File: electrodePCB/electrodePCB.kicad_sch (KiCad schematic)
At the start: 18 parts, among them J1 Conn_01x16_Pin, U1 TMP119AIYBGR

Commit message: still in the middle of it, but added the 20p, 2 additional heaters (including adjustable postition) and begining to define pinout
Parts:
- removed J1: Conn_01x16_Pin, MOLEX FPC:CON_5034801600_MOL, symbol Connector:Conn_01x16_Pin
- added J1: Conn_01x20, 5034802000 FPC Molex:CON_5034802000_MOL, symbol Connector_Generic:Conn_01x20
- added R10, R8, R9: R_US, Resistor_SMD:R_0603_1608Metric, symbol Device:R_US
- R2: renamed from R6; footprint Resistor_SMD:R_2512_6332Metric_Pad1.40x3.35mm_HandSolder -> Resistor_SMD:adjustable
- renumbered E1 to E0, E2 to E1, E3 to E2, E4 to E3, E5 to E4, E6 to E5, R7 to R3, R3 to R4, R2 to R5, R4 to R6, R5 to R7
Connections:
- net +3V3: now also J1.11 (Pin_11)
- net GND: now also R1.2, R2.2, R3.2, J1.14 (Pin_14), J1.15 (Pin_15), J1.17 (Pin_17), J1.19 (Pin_19), R10.1, R8.1, R9.1
- net SCL: now also J1.13 (Pin_13)
- net SDA: now also J1.12 (Pin_12)
- net at E0.1 (Pin_1): now also J1.1 (Pin_1), R8.2
- net at E2.1 (Pin_1): now also J1.3 (Pin_3), R10.2
- net at E1.1 (Pin_1): now also J1.2 (Pin_2), R9.2
- net at E3.1 (Pin_1): now also J1.4 (Pin_4)
- net at R1.1: now also J1.20 (Pin_20)
- net at S1.1 (Pin_1): now also J1.7 (Pin_7)
- net at S1.2 (Pin_2): now also J1.8 (Pin_8)
- net at S1.3 (Pin_3): now also J1.9 (Pin_9)
- net at S1.4 (Pin_4): now also J1.10 (Pin_10)
- net at E4.1 (Pin_1): now also J1.5 (Pin_5)
- net at E5.1 (Pin_1): now also J1.6 (Pin_6)
- net at R3.1: now also J1.16 (Pin_16)
- net at R2.1: now also J1.18 (Pin_18)
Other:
- moved on the sheet: R1, R2, R3

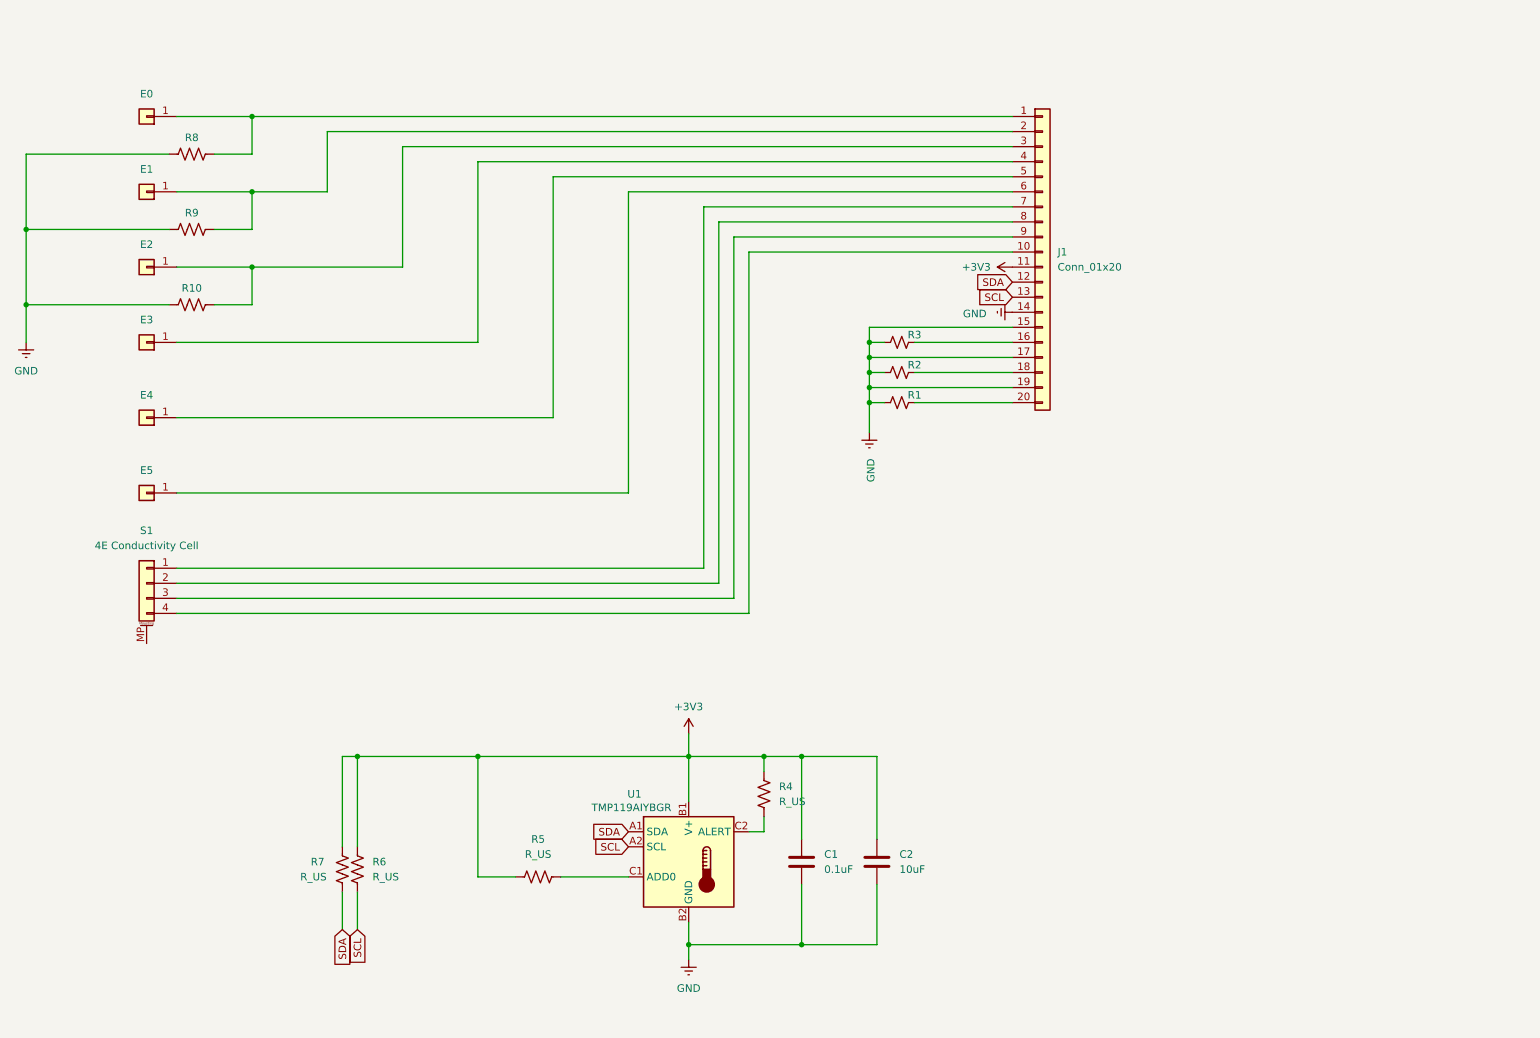
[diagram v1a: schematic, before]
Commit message: bunch of routing, adapted interconnect pinout to accomedate routing. Added GND plane.
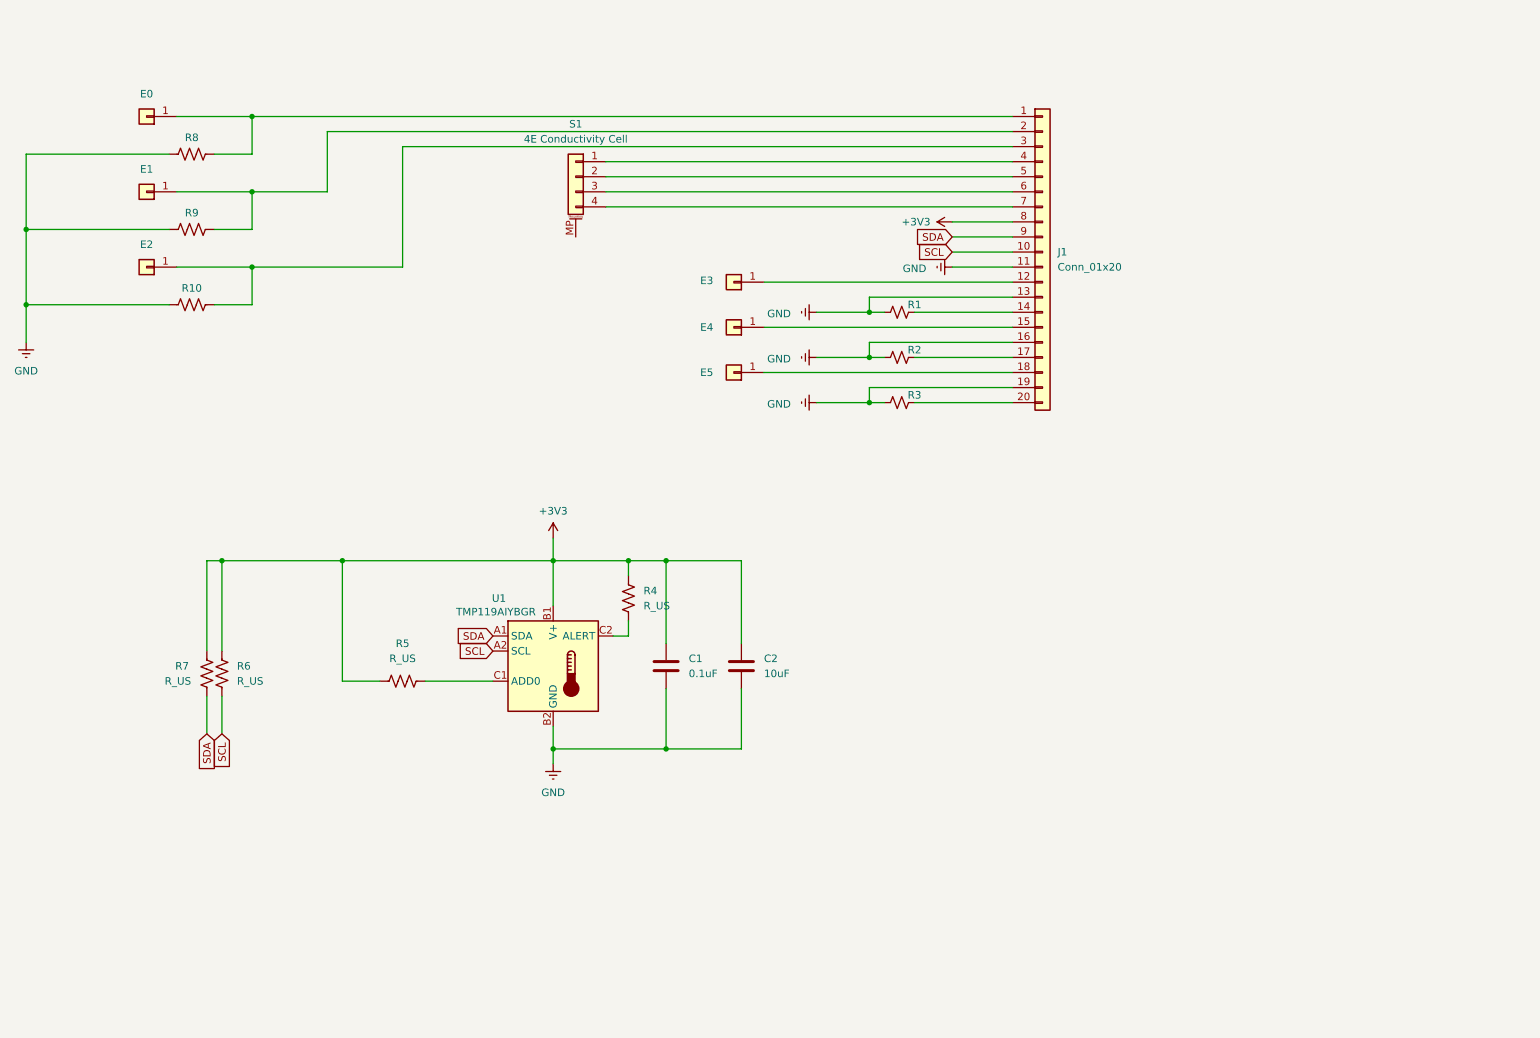
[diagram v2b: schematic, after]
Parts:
- R6, R7: footprint Resistor_SMD:R_0603_1608Metric -> Resistor_SMD:R_0402_1005Metric
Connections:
- net +3V3: now also J1.8 (Pin_8); no longer J1.11 (Pin_11)
- net GND: now also J1.11 (Pin_11), J1.13 (Pin_13), J1.16 (Pin_16); no longer J1.14 (Pin_14), J1.15 (Pin_15), J1.17 (Pin_17)
- net SCL: now also J1.10 (Pin_10); no longer J1.13 (Pin_13)
- net SDA: now also J1.9 (Pin_9); no longer J1.12 (Pin_12)
- net at E3.1 (Pin_1): now also J1.12 (Pin_12); no longer J1.4 (Pin_4)
- net at R1.1: now also J1.14 (Pin_14); no longer J1.20 (Pin_20)
- net at E4.1 (Pin_1): now also J1.15 (Pin_15); no longer J1.5 (Pin_5)
- net at R3.1: now also J1.20 (Pin_20); no longer J1.16 (Pin_16)
- net at R2.1: now also J1.17 (Pin_17); no longer J1.18 (Pin_18)
- net at E5.1 (Pin_1): now also J1.18 (Pin_18); no longer J1.6 (Pin_6)
- net at S1.4 (Pin_4): now also J1.7 (Pin_7); no longer J1.10 (Pin_10)
- net at S1.1 (Pin_1): now also J1.4 (Pin_4); no longer J1.7 (Pin_7)
- net at S1.2 (Pin_2): now also J1.5 (Pin_5); no longer J1.8 (Pin_8)
- net at S1.3 (Pin_3): now also J1.6 (Pin_6); no longer J1.9 (Pin_9)
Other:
- moved on the sheet: C1, C2, E3, E4, E5, R1, R2, R3, R4, R5, R6, R7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

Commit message: routing, routing, routing. We removed one of the three heaters and decided to displace the other two and route to rings around the electrodes. I verified the temperature sensor is work!
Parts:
- removed R2: R_Small_US, Resistor_SMD:adjustable, symbol Device:R_Small_US
- added J2: qwiic, Connector_JST:JST_SH_BM04B-SRSS-TB_1x04-1MP_P1.00mm_Vertical, symbol Connector_Generic_MountingPin:Conn_01x04_MountingPin
- J1: value Conn_01x20 -> FPC 20p
- R1, R3: footprint Resistor_SMD:R_2512_6332Metric_Pad1.40x3.35mm_HandSolder -> Resistor_SMD:R_2010_5025Metric
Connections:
- net +3V3: now also J2.2 (Pin_2)
- net GND: now also J1.15 (Pin_15), J2.1 (Pin_1); no longer J1.13 (Pin_13), J1.16 (Pin_16)
- net SCL: now also J2.4 (Pin_4)
- net SDA: now also J2.3 (Pin_3)
- net at E3.1 (Pin_1): now also J1.14 (Pin_14); no longer J1.12 (Pin_12)
- net at R1.1: now also J1.18 (Pin_18); no longer J1.14 (Pin_14)
- net at E4.1 (Pin_1): now also J1.17 (Pin_17); no longer J1.15 (Pin_15)
- net at R3.1: now also J1.16 (Pin_16); no longer J1.20 (Pin_20)
- net at E5.1 (Pin_1): now also J1.20 (Pin_20); no longer J1.18 (Pin_18)
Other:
- moved on the sheet: E0, E1, E2, E3, E4, E5, J1, R1, R10, R3, R8, R9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

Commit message: routing and more routing. still working, but add thermal rings. added qwiic.
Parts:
- removed C2: 10uF, Capacitor_SMD:C_0603_1608Metric, symbol Device:C
- R4, R5: footprint Resistor_SMD:R_0603_1608Metric -> Resistor_SMD:R_0402_1005Metric
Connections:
- net +3V3: now also J1.10 (Pin_10); no longer J1.8 (Pin_8)
- net SCL: now also J1.8 (Pin_8); no longer J1.10 (Pin_10)
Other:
- moved on the sheet: J2

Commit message: roughly finalized layout. Might tidy up the GND plane with some keep outs
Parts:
- R0: renamed from R8; value R_US -> 0 ohm
- R4, R7: value R_US -> 10k
- R6: renamed from R5; value R_US -> 10k
- R8: renamed from R6; value R_US -> 10k
- renumbered R9 to R1, R10 to R2, R1 to R5
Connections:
- net at E3.1 (Pin_1): now also J1.12 (Pin_12); no longer J1.14 (Pin_14)
- net at J1.18 (Pin_18), R5.1: now also J1.17 (Pin_17)
- net at E4.1 (Pin_1): now also J1.16 (Pin_16); no longer J1.17 (Pin_17)
- net at R3.1: now also J1.13 (Pin_13), J1.14 (Pin_14); no longer J1.16 (Pin_16)
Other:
- note added: "3 typical reference electrodes (E0-E2)"
- note added: "4E conductivity cell"
- note added: "Electrodes (E3-E5) typically ISEs"
- note added: "Main interconnect"
- note added: "Qwiic Connector"
- note added: "Temperature Sensor"
- company: (none) -> William Pardis
- title: (none) -> electrodePCB
- moved on the sheet: C1, E0, E1, E2, E3, E4, E5, J1, J2, R0, R1, R2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

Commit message: labeling of the Cond Cell
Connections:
- net force 1: now reaches J1.4 (Pin_4), S1.1 (Pin_1)
- net Sense 1: now reaches J1.5 (Pin_5), S1.2 (Pin_2)
- net Sense 2: now reaches J1.6 (Pin_6), S1.3 (Pin_3)
- net force 2: now reaches J1.7 (Pin_7), S1.4 (Pin_4)
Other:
- note removed: "4E conductivity cell"
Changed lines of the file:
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@@
-		)
-	)
-	(text "4E conductivity cell"
-		(exclude_from_sim no)
-		(at 112.522 80.772 0)
-		(effects
-			(font
-				(face "Arial Black")
-				(size 2.54 2.54)
-				(bold yes)
-			)
-			(justify left)
 		)
 	)
@@
 			(width 0)
 			(type default)
+		)
+	)
+	(label "force 2"
+		(at 149.86 71.12 0)
+		(effects
+			(font
+				(size 1.27 1.27)
+			)
+			(justify left bottom)
+		)
+	)
+	(label "Sense 1"
+		(at 167.64 66.04 0)
+		(effects
+			(font
+				(size 1.27 1.27)
+			)
+			(justify left bottom)
+		)
+	)
+	(label "Sense 2"
+		(at 167.64 68.58 0)
+		(effects
+			(font
+				(size 1.27 1.27)
+			)
+			(justify left bottom)
+		)
+	)
+	(label "force 1"
+		(at 149.86 63.5 0)
+		(effects
+			(font
+				(size 1.27 1.27)
+			)
+			(justify left bottom)
 		)
 	)
@@
 		(on_board yes)
 		(dnp no)
-		(fields_autoplaced yes)
 		(property "Reference" "S1"
-			(at 130.81 57.15 0)
+			(at 126.746 67.564 0)
 			(effects
 				(font
@@
 		)
 		(property "Value" "4E Conductivity Cell"
-			(at 130.81 59.69 0)
-			(effects
-				(font
+			(at 130.81 77.978 0)
+			(effects
+				(font
